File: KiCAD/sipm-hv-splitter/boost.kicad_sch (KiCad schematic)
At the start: 52 parts, among them Q3 BSS138, Q4 BSS138, Q5 BSS138, U2 LT3014xS5, U3 INA201, U4 AD5270

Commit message: working on SiPM power supply schem
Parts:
- C1: renamed from C6; value 0.1uF -> 4.7uF; footprint (none) -> Capacitor_SMD:C_0603_1608Metric_Pad1.08x0.95mm_HandSolder
- C10: renamed from C8; value 0.1uF -> 0.1uF 100V; footprint (none) -> Capacitor_SMD:C_0603_1608Metric_Pad1.08x0.95mm_HandSolder
- C2: value 0.1uF -> 1.0uF; footprint (none) -> Capacitor_SMD:C_0603_1608Metric_Pad1.08x0.95mm_HandSolder
- C3: renamed from C1; value 0.1uF -> 1.0uF; footprint (none) -> Capacitor_SMD:C_0603_1608Metric_Pad1.08x0.95mm_HandSolder
- C4: renamed from C3; value C -> 12nF; footprint (none) -> Capacitor_SMD:C_0603_1608Metric_Pad1.08x0.95mm_HandSolder
- C6: renamed from C10; value C -> 1.0uF
- C7: renamed from C4; value C -> 22nF; footprint (none) -> Capacitor_SMD:C_0603_1608Metric_Pad1.08x0.95mm_HandSolder
- C8: renamed from C5; value C -> 56pF; footprint (none) -> Capacitor_SMD:C_0603_1608Metric_Pad1.08x0.95mm_HandSolder
- C9: renamed from C7; value 3.3uF -> 4.7uF 100V; footprint (none) -> Capacitor_SMD:C_0603_1608Metric_Pad1.08x0.95mm_HandSolder
- D1: value D_Schottky -> MBR1H100SFT3G; footprint (none) -> Diode_SMD:Nexperia_CFP3_SOD-123W; CatNo (none) -> MBR1H100SFT3GOSCT-ND; MfgNo (none) -> MBR1H100SFT3G
- L1: footprint (none) -> my_SMT_Ind:WE-TPC-ind; CatNo (none) -> 732-2617-1-ND; MfgNo (none) -> 744025100
- R10: renamed from R14; value R -> 100; CatNo 311-0.0GRCT-ND -> (none); MfgNo RC0603JR-070RL -> (none)
- R12: renamed from R3; value R_US -> 3.16k; footprint (none) -> Resistor_SMD:R_0603_1608Metric_Pad0.98x0.95mm_HandSolder
- R13: renamed from R4; value R_US -> 150k; footprint (none) -> Resistor_SMD:R_0603_1608Metric_Pad0.98x0.95mm_HandSolder
- R14: renamed from R5; value R_US -> 2.49k; footprint (none) -> Resistor_SMD:R_0603_1608Metric_Pad0.98x0.95mm_HandSolder
- R18: renamed from R9; value 200k 1% -> 510k 1%; CatNo 311-100KHRCT-ND -> (none); MfgNo RC0603FR-07100KL -> (none)
- R19: renamed from R10; value 10.0k 1% -> 24.0k 1%; CatNo 311-10.0KHRCT-ND -> (none); MfgNo RC0603FR-0710KL -> (none)
- R6: renamed from R2; value R_US -> 9.76k; footprint (none) -> Resistor_SMD:R_0603_1608Metric_Pad0.98x0.95mm_HandSolder
- R7: renamed from R18; footprint (none) -> Resistor_SMD:R_0603_1608Metric_Pad0.98x0.95mm_HandSolder
- R8: renamed from R13; value R -> 100; CatNo 311-0.0GRCT-ND -> (none); MfgNo RC0603JR-070RL -> (none)
- U3: renamed from U1; value ~ -> LM51581; footprint (none) -> my_Boost_QFN:QFN-16_EP_3x3_Pitch0.5mm
- renumbered C9 to C11, C11 to C12, C12 to C13, C13 to C14, C14 to C15, C9 to C5, Q5 to Q1, Q3 to Q2, Q4 to Q3, R7 to R11, R6 to R15, R8 to R16, R9 to R17, R11 to R2, R17 to R20, R12 to R3, R16 to R4, R15 to R5, R6 to R9, TP7 to TP1, TP5 to TP2, TP8 to TP3, TP3 to TP4, TP2 to TP5, TP1 to TP6, TP6 to TP7, TP4 to TP8, U3 to U2, U2 to U4, U4 to U5

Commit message: starting placement
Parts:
- C4: value 12nF -> 0.1uF
- R6: value 9.76k -> 10k
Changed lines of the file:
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@@
 			)
 		)
-		(property "Value" "9.76k"
+		(property "Value" "10k"
 			(at 55.88 172.7199 0)
 			(effects
@@
 			)
 		)
-		(property "Value" "12nF"
+		(property "Value" "0.1uF"
 			(at 64.77 172.7262 0)
 			(effects

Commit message: add ISP
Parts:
- C10: footprint Capacitor_SMD:C_0603_1608Metric_Pad1.08x0.95mm_HandSolder -> Capacitor_SMD:C_1206_3216Metric_Pad1.33x1.80mm_HandSolder
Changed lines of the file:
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@@
 			)
 		)
-		(property "Footprint" "Capacitor_SMD:C_0603_1608Metric_Pad1.08x0.95mm_HandSolder"
+		(property "Footprint" "Capacitor_SMD:C_1206_3216Metric_Pad1.33x1.80mm_HandSolder"
 			(at 133.35 146.05 0)
 			(effects

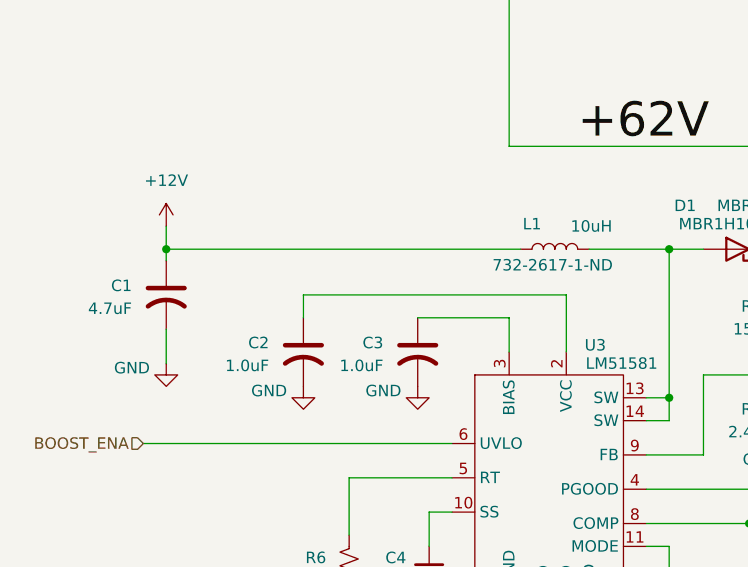
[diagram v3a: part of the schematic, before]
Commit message: working on 2.5 in placement
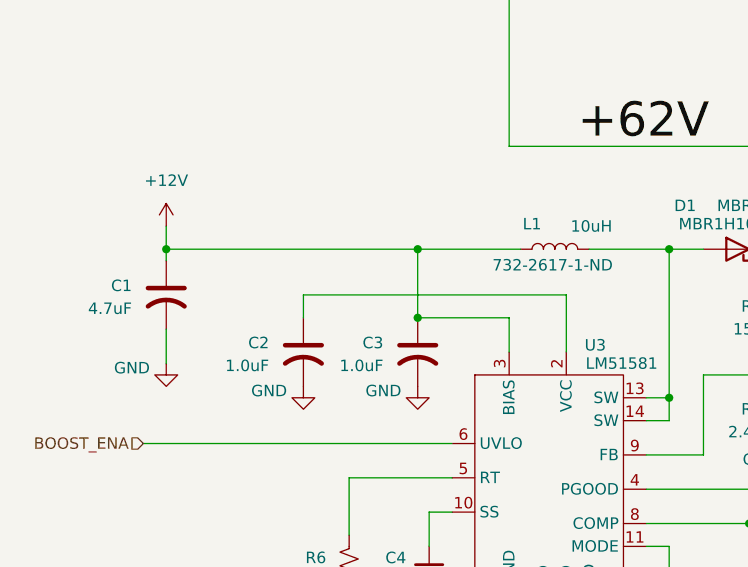
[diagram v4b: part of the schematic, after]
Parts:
- C10: footprint Capacitor_SMD:C_1206_3216Metric_Pad1.33x1.80mm_HandSolder -> Capacitor_SMD:C_0603_1608Metric_Pad1.08x0.95mm_HandSolder
- C9: footprint Capacitor_SMD:C_0603_1608Metric_Pad1.08x0.95mm_HandSolder -> Capacitor_SMD:C_1206_3216Metric_Pad1.33x1.80mm_HandSolder
- R9: footprint Resistor_SMD:R_0603_1608Metric_Pad0.98x0.95mm_HandSolder -> Resistor_SMD:R_1206_3216Metric_Pad1.30x1.75mm_HandSolder
- TP1, TP2, TP3, TP4, TP5, TP6, TP7, TP8: footprint my_tp:tp_SMT_label2 -> TestPoint:TestPoint_Pad_D2.0mm
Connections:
- net +12V: now also C3.1, U3.3 (BIAS)
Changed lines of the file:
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@@
 	)
 	(junction
+		(at 66.04 143.51)
+		(diameter 0)
+		(color 0 0 0 0)
+	)
+	(junction
 		(at 233.68 49.53)
 		(diameter 0)
@@
 	)
 	(junction
+		(at 66.04 135.89)
+		(diameter 0)
+		(color 0 0 0 0)
+	)
+	(junction
 		(at 243.84 41.91)
 		(diameter 0)
@@
 	(wire
 		(pts
+			(xy 66.04 135.89) (xy 77.47 135.89)
+		)
+		(stroke
+			(width 0)
+			(type default)
+		)
+	)
+	(wire
+		(pts
 			(xy 53.34 140.97) (xy 82.55 140.97)
 		)
@@
 	(wire
 		(pts
-			(xy 38.1 135.89) (xy 77.47 135.89)
+			(xy 38.1 135.89) (xy 66.04 135.89)
 		)
 		(stroke
@@
 	(wire
 		(pts
+			(xy 66.04 135.89) (xy 66.04 143.51)
+		)
+		(stroke
+			(width 0)
+			(type default)
+		)
+	)
+	(wire
+		(pts
 			(xy 53.34 44.45) (xy 53.34 66.04)
 		)
@@
 			)
 		)
-		(property "Footprint" "my_tp:tp_SMT_label2"
+		(property "Footprint" "TestPoint:TestPoint_Pad_D2.0mm"
 			(at 248.92 38.1 0)
 			(effects
@@
 			)
 		)
-		(property "Footprint" "Capacitor_SMD:C_1206_3216Metric_Pad1.33x1.80mm_HandSolder"
+		(property "Footprint" "Capacitor_SMD:C_0603_1608Metric_Pad1.08x0.95mm_HandSolder"
 			(at 133.35 146.05 0)
 			(effects
@@
 			)
 		)
-		(property "Footprint" "my_tp:tp_SMT_label2"
+		(property "Footprint" "TestPoint:TestPoint_Pad_D2.0mm"
 			(at 104.14 58.42 0)
 			(effects
@@
 			)
 		)
-		(property "Footprint" "my_tp:tp_SMT_label2"
+		(property "Footprint" "TestPoint:TestPoint_Pad_D2.0mm"
 			(at 81.28 88.9 0)
 			(effects
@@
 			)
 		)
-		(property "Footprint" "my_tp:tp_SMT_label2"
+		(property "Footprint" "TestPoint:TestPoint_Pad_D2.0mm"
 			(at 236.22 113.03 0)
 			(effects
@@
 			)
 		)
-		(property "Footprint" "my_tp:tp_SMT_label2"
+		(property "Footprint" "TestPoint:TestPoint_Pad_D2.0mm"
 			(at 228.6 52.07 0)
 			(effects
@@
 			)
 		)
-		(property "Footprint" "Resistor_SMD:R_0603_1608Metric_Pad0.98x0.95mm_HandSolder"
+		(property "Footprint" "Resistor_SMD:R_1206_3216Metric_Pad1.30x1.75mm_HandSolder"
 			(at 91.694 97.536 90)
 			(effects
@@
 			)
 		)
-		(property "Footprint" "Capacitor_SMD:C_0603_1608Metric_Pad1.08x0.95mm_HandSolder"
+		(property "Footprint" "Capacitor_SMD:C_1206_3216Metric_Pad1.33x1.80mm_HandSolder"
 			(at 120.65 146.05 0)
 			(effects
@@
 			)
 		)
-		(property "Footprint" "my_tp:tp_SMT_label2"
+		(property "Footprint" "TestPoint:TestPoint_Pad_D2.0mm"
 			(at 185.42 59.69 0)
 			(effects
@@
 			)
 		)
-		(property "Footprint" "my_tp:tp_SMT_label2"
+		(property "Footprint" "TestPoint:TestPoint_Pad_D2.0mm"
 			(at 33.02 41.91 0)
 			(effects
@@
 			)
 		)
-		(property "Footprint" "my_tp:tp_SMT_label2"
+		(property "Footprint" "TestPoint:TestPoint_Pad_D2.0mm"
 			(at 109.22 88.9 0)
 			(effects

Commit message: routing madness
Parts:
- C15: now fitted
- TP1, TP2, TP3, TP4, TP5, TP6, TP7, TP8: footprint TestPoint:TestPoint_Pad_D2.0mm -> TestPoint:TestPoint_Pad_D1.0mm; now fitted; now left out of the parts list
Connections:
- net V62_IN: now reaches C11.1, R10.2, R9.2, TP4.1, U4.1 (VIN)
- net +62V renamed 62V
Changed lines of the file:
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@@
 		)
 	)
+	(label "V62_IN"
+		(at 114.3 92.71 0)
+		(effects
+			(font
+				(size 1.27 1.27)
+			)
+			(justify left bottom)
+		)
+	)
 	(label "IMON"
 		(at 46.99 48.26 0)
@@
 		)
 	)
-	(label "+62V"
+	(label "62V"
 		(at 83.82 124.46 0)
 		(effects
@@
 		(unit 1)
 		(exclude_from_sim no)
-		(in_bom yes)
+		(in_bom no)
 		(on_board yes)
-		(dnp yes)
+		(dnp no)
 		(property "Reference" "TP8"
 			(at 238.506 32.258 0)
@@
 			)
 		)
-		(property "Footprint" "TestPoint:TestPoint_Pad_D2.0mm"
+		(property "Footprint" "TestPoint:TestPoint_Pad_D1.0mm"
 			(at 248.92 38.1 0)
 			(effects
@@
 		(in_bom no)
 		(on_board yes)
-		(dnp yes)
+		(dnp no)
 		(property "Reference" "C15"
 			(at 236.22 93.9799 0)
@@
 		(unit 1)
 		(exclude_from_sim no)
-		(in_bom yes)
+		(in_bom no)
 		(on_board yes)
-		(dnp yes)
+		(dnp no)
 		(property "Reference" "TP3"
 			(at 101.6 62.9921 0)
@@
 			)
 		)
-		(property "Footprint" "TestPoint:TestPoint_Pad_D2.0mm"
+		(property "Footprint" "TestPoint:TestPoint_Pad_D1.0mm"
 			(at 104.14 58.42 0)
 			(effects
@@
 		(unit 1)
 		(exclude_from_sim no)
-		(in_bom yes)
+		(in_bom no)
 		(on_board yes)
-		(dnp yes)
+		(dnp no)
 		(property "Reference" "TP2"
 			(at 71.628 88.392 0)
@@
 			)
 		)
-		(property "Footprint" "TestPoint:TestPoint_Pad_D2.0mm"
+		(property "Footprint" "TestPoint:TestPoint_Pad_D1.0mm"
 			(at 81.28 88.9 0)
 			(effects
@@
 		(unit 1)
 		(exclude_from_sim no)
-		(in_bom yes)
+		(in_bom no)
 		(on_board yes)
-		(dnp yes)
+		(dnp no)
 		(fields_autoplaced yes)
 		(property "Reference" "TP6"
@@
 			)
 		)
-		(property "Footprint" "TestPoint:TestPoint_Pad_D2.0mm"
+		(property "Footprint" "TestPoint:TestPoint_Pad_D1.0mm"
 			(at 236.22 113.03 0)
 			(effects
@@
 		(unit 1)
 		(exclude_from_sim no)
-		(in_bom yes)
+		(in_bom no)
 		(on_board yes)
-		(dnp yes)
+		(dnp no)
 		(property "Reference" "TP7"
 			(at 239.776 54.356 0)
@@
 			)
 		)
-		(property "Footprint" "TestPoint:TestPoint_Pad_D2.0mm"
+		(property "Footprint" "TestPoint:TestPoint_Pad_D1.0mm"
 			(at 228.6 52.07 0)
 			(effects
@@
 		(unit 1)
 		(exclude_from_sim no)
-		(in_bom yes)
+		(in_bom no)
 		(on_board yes)
-		(dnp yes)
+		(dnp no)
 		(fields_autoplaced yes)
 		(property "Reference" "TP5"
@@
 			)
 		)
-		(property "Footprint" "TestPoint:TestPoint_Pad_D2.0mm"
+		(property "Footprint" "TestPoint:TestPoint_Pad_D1.0mm"
 			(at 185.42 59.69 0)
 			(effects
@@
 		(unit 1)
 		(exclude_from_sim no)
-		(in_bom yes)
+		(in_bom no)
 		(on_board yes)
-		(dnp yes)
+		(dnp no)
 		(property "Reference" "TP1"
 			(at 35.56 37.3379 0)
@@
 			)
 		)
-		(property "Footprint" "TestPoint:TestPoint_Pad_D2.0mm"
+		(property "Footprint" "TestPoint:TestPoint_Pad_D1.0mm"
 			(at 33.02 41.91 0)
 			(effects
@@
 		(unit 1)
 		(exclude_from_sim no)
-		(in_bom yes)
+		(in_bom no)
 		(on_board yes)
-		(dnp yes)
+		(dnp no)
 		(property "Reference" "TP4"
 			(at 99.568 87.63 0)
@@
 			)
 		)
-		(property "Footprint" "TestPoint:TestPoint_Pad_D2.0mm"
+		(property "Footprint" "TestPoint:TestPoint_Pad_D1.0mm"
 			(at 109.22 88.9 0)
 			(effects

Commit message: working on bias filter changes
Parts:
- C1, C10, C2, C3, C9: symbol Device:C_US -> Device:C
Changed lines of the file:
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@@
 	)
 	(symbol
-		(lib_id "Device:C_US")
+		(lib_id "Device:C")
 		(at 133.35 146.05 0)
 		(unit 1)
@@
 		)
 		(property "Footprint" "Capacitor_SMD:C_0603_1608Metric_Pad1.08x0.95mm_HandSolder"
-			(at 133.35 146.05 0)
+			(at 134.3152 149.86 0)
 			(effects
 				(font
@@
 			)
 		)
-		(property "Datasheet" ""
+		(property "Datasheet" "~"
 			(at 133.35 146.05 0)
 			(effects
@@
 			)
 		)
-		(property "Description" "capacitor, US symbol"
+		(property "Description" "Unpolarized capacitor"
 			(at 133.35 146.05 0)
 			(effects
@@
 	)
 	(symbol
-		(lib_id "Device:C_US")
+		(lib_id "Device:C")
 		(at 38.1 140.97 0)
 		(unit 1)
@@
 		)
 		(property "Footprint" "Capacitor_SMD:C_0603_1608Metric_Pad1.08x0.95mm_HandSolder"
-			(at 38.1 140.97 0)
+			(at 39.0652 144.78 0)
 			(effects
 				(font
@@
 			)
 		)
-		(property "Datasheet" ""
+		(property "Datasheet" "~"
 			(at 38.1 140.97 0)
 			(effects
@@
 			)
 		)
-		(property "Description" "capacitor, US symbol"
+		(property "Description" "Unpolarized capacitor"
 			(at 38.1 140.97 0)
 			(effects
@@
 	)
 	(symbol
-		(lib_id "Device:C_US")
+		(lib_id "Device:C")
 		(at 120.65 146.05 0)
 		(unit 1)
@@
 		)
 		(property "Footprint" "Capacitor_SMD:C_1206_3216Metric_Pad1.33x1.80mm_HandSolder"
-			(at 120.65 146.05 0)
+			(at 121.6152 149.86 0)
 			(effects
 				(font
@@
 			)
 		)
-		(property "Datasheet" ""
+		(property "Datasheet" "~"
 			(at 120.65 146.05 0)
 			(effects
@@
 			)
 		)
-		(property "Description" "capacitor, US symbol"
+		(property "Description" "Unpolarized capacitor"
 			(at 120.65 146.05 0)
 			(effects
@@
 	)
 	(symbol
-		(lib_id "Device:C_US")
+		(lib_id "Device:C")
 		(at 53.34 147.32 0)
 		(unit 1)
@@
 		)
 		(property "Footprint" "Capacitor_SMD:C_0603_1608Metric_Pad1.08x0.95mm_HandSolder"
-			(at 53.34 147.32 0)
+			(at 54.3052 151.13 0)
 			(effects
 				(font
@@
 			)
 		)
-		(property "Datasheet" ""
+		(property "Datasheet" "~"
 			(at 53.34 147.32 0)
 			(effects
@@
 			)
 		)
-		(property "Description" "capacitor, US symbol"
+		(property "Description" "Unpolarized capacitor"
 			(at 53.34 147.32 0)
 			(effects
@@
 	)
 	(symbol
-		(lib_id "Device:C_US")
+		(lib_id "Device:C")
 		(at 66.04 147.32 0)
 		(unit 1)
@@
 		)
 		(property "Footprint" "Capacitor_SMD:C_0603_1608Metric_Pad1.08x0.95mm_HandSolder"
-			(at 66.04 147.32 0)
+			(at 67.0052 151.13 0)
 			(effects
 				(font
@@
 			)
 		)
-		(property "Datasheet" ""
+		(property "Datasheet" "~"
 			(at 66.04 147.32 0)
 			(effects
@@
 			)
 		)
-		(property "Description" "capacitor, US symbol"
+		(property "Description" "Unpolarized capacitor"
 			(at 66.04 147.32 0)
 			(effects

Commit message: working on BOM
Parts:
- C1: CatNo (none) -> 1276-1784-1-ND; MfgNo (none) -> CL10A475KO8NNNC
- C10: CatNo (none) -> 1276-6807-1-ND; MfgNo (none) -> CL10B104KC8NNNC
- C13, C5: CatNo 399-C0603C103M4REC7411CT-ND -> 478-KGF15AR71H103MTCT-ND; MfgNo C0603C103M4REC7411 -> 06035C103MAZ2A
- C2, C3, C6: CatNo (none) -> 1276-1019-1-ND; MfgNo (none) -> CL10B105KO8NNNC
- C4: CatNo (none) -> 311-1088-1-ND; MfgNo (none) -> CC0603KRX7R7BB104
- C7: CatNo (none) -> 1292-1415-1-ND; MfgNo (none) -> 0603B223K160CT
- C8: CatNo (none) -> 478-600S560JT250XT4KCT-ND; MfgNo (none) -> 600S560JT250XT4K
- C9: CatNo (none) -> 490-18620-1-ND; MfgNo (none) -> GRM31CC72A475KE11L
- R10, R8: CatNo (none) -> P100HCT-ND; MfgNo (none) -> ERJ-3EKF1000V
- R16, R5: value 10.0k 1% -> 10k
- R6: CatNo (none) -> 311-10.0KHRCT-ND; MfgNo (none) -> RC0603FR-0710KL
- R7: CatNo (none) -> 541-100KHCT-ND; MfgNo (none) -> CRCW0603100KFKEA
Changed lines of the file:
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@@
 			)
 		)
-		(property "MfgNo" "C0603C103M4REC7411"
+		(property "MfgNo" "06035C103MAZ2A"
 			(at 199.39 97.79 0)
 			(effects
@@
 			)
 		)
-		(property "CatNo" "399-C0603C103M4REC7411CT-ND"
+		(property "CatNo" "478-KGF15AR71H103MTCT-ND"
 			(at 199.39 97.79 0)
 			(effects
@@
 			)
 		)
+		(property "CatNo" "478-600S560JT250XT4KCT-ND"
+			(at 107.95 177.8 0)
+			(effects
+				(font
+					(size 1.27 1.27)
+				)
+				(hide yes)
+			)
+		)
+		(property "MfgNo" "600S560JT250XT4K"
+			(at 107.95 177.8 0)
+			(effects
+				(font
+					(size 1.27 1.27)
+				)
+				(hide yes)
+			)
+		)
 		(pin "1"
 		)
@@
 			)
 		)
+		(property "CatNo" "311-10.0KHRCT-ND"
+			(at 58.42 171.45 0)
+			(effects
+				(font
+					(size 1.27 1.27)
+				)
+				(hide yes)
+			)
+		)
+		(property "MfgNo" "RC0603FR-0710KL"
+			(at 58.42 171.45 0)
+			(effects
+				(font
+					(size 1.27 1.27)
+				)
+				(hide yes)
+			)
+		)
 		(pin "1"
 		)
@@
 			)
 		)
+		(property "CatNo" "1292-1415-1-ND"
+			(at 102.87 182.88 0)
+			(effects
+				(font
+					(size 1.27 1.27)
+				)
+				(hide yes)
+			)
+		)
+		(property "MfgNo" "0603B223K160CT"
+			(at 102.87 182.88 0)
+			(effects
+				(font
+					(size 1.27 1.27)
+				)
+				(hide yes)
+			)
+		)
 		(pin "1"
 		)
@@
 			)
 		)
+		(property "CatNo" "1276-6807-1-ND"
+			(at 133.35 146.05 0)
+			(effects
+				(font
+					(size 1.27 1.27)
+				)
+				(hide yes)
+			)
+		)
+		(property "MfgNo" "CL10B104KC8NNNC"
+			(at 133.35 146.05 0)
+			(effects
+				(font
+					(size 1.27 1.27)
+				)
+				(hide yes)
+			)
+		)
 		(pin "1"
 		)
@@
 			)
 		)
-		(property "MfgNo" ""
+		(property "MfgNo" "ERJ-3EKF1000V"
 			(at 95.25 77.47 0)
 			(effects
@@
 			)
 		)
-		(property "CatNo" ""
+		(property "CatNo" "P100HCT-ND"
 			(at 95.25 77.47 0)
 			(effects
@@
 			)
 		)
+		(property "CatNo" "1276-1784-1-ND"
+			(at 38.1 140.97 0)
+			(effects
+				(font
+					(size 1.27 1.27)
+				)
+				(hide yes)
+			)
+		)
+		(property "MfgNo" "CL10A475KO8NNNC"
+			(at 38.1 140.97 0)
+			(effects
+				(font
+					(size 1.27 1.27)
+				)
+				(hide yes)
+			)
+		)
 		(pin "1"
 		)
@@
 			)
 		)
-		(property "MfgNo" ""
+		(property "MfgNo" "ERJ-3EKF1000V"
 			(at 87.63 77.47 0)
 			(effects
@@
 			)
 		)
-		(property "CatNo" ""
+		(property "CatNo" "P100HCT-ND"
 			(at 87.63 77.47 0)
 			(effects
@@
 			)
 		)
-		(property "MfgNo" "C0603C103M4REC7411"
+		(property "MfgNo" "06035C103MAZ2A"
 			(at 76.2 31.75 0)
 			(effects
@@
 			)
 		)
-		(property "CatNo" "399-C0603C103M4REC7411CT-ND"
+		(property "CatNo" "478-KGF15AR71H103MTCT-ND"
 			(at 76.2 31.75 0)
 			(effects
@@
 			)
 		)
+		(property "CatNo" "490-18620-1-ND"
+			(at 120.65 146.05 0)
+			(effects
+				(font
+					(size 1.27 1.27)
+				)
+				(hide yes)
+			)
+		)
+		(property "MfgNo" "GRM31CC72A475KE11L"
+			(at 120.65 146.05 0)
+			(effects
+				(font
+					(size 1.27 1.27)
+				)
+				(hide yes)
+			)
+		)
 		(pin "1"
 		)
@@
 		(fields_autoplaced yes)
 		(property "Reference" "R16"
-			(at 119.38 43.1799 0)
+			(at 124.46 43.1799 0)
 			(effects
 				(font
 					(size 1.27 1.27)
 				)
-				(justify left)
+				(justify right)
 			)
 		)
-		(property "Value" "10.0k 1%"
-			(at 119.38 45.7199 0)
+		(property "Value" "10k"
+			(at 124.46 45.7199 0)
 			(effects
 				(font
 					(size 1.27 1.27)
 				)
-				(justify left)
+				(justify right)
 			)
 		)
@@
 			)
 		)
+		(property "CatNo" "311-1088-1-ND"
+			(at 67.31 171.45 0)
+			(effects
+				(font
+					(size 1.27 1.27)
+				)
+				(hide yes)
+			)
+		)
+		(property "MfgNo" "CC0603KRX7R7BB104"
+			(at 67.31 171.45 0)
+			(effects
+				(font
+					(size 1.27 1.27)
+				)
+				(hide yes)
+			)
+		)
 		(pin "1"
 		)
@@
 			)
 		)
+		(property "CatNo" "1276-1019-1-ND"
+			(at 53.34 147.32 0)
+			(effects
+				(font
+					(size 1.27 1.27)
+				)
+				(hide yes)
+			)
+		)
+		(property "MfgNo" "CL10B105KO8NNNC"
+			(at 53.34 147.32 0)
+			(effects
+				(font
+					(size 1.27 1.27)
+				)
+				(hide yes)
+			)
+		)
 		(pin "1"
 		)
@@
 			)
 		)
+		(property "CatNo" "541-100KHCT-ND"
+			(at 60.96 101.6 0)
+			(effects
+				(font
+					(size 1.27 1.27)
+				)
+				(hide yes)
+			)
+		)
+		(property "MfgNo" "CRCW0603100KFKEA"
+			(at 60.96 101.6 0)
+			(effects
+				(font
+					(size 1.27 1.27)
+				)
+				(hide yes)
+			)
+		)
 		(pin "1"
 		)
@@
 			)
 		)
+		(property "CatNo" "1276-1019-1-ND"
+			(at 66.04 147.32 0)
+			(effects
+				(font
+					(size 1.27 1.27)
+				)
+				(hide yes)
+			)
+		)
+		(property "MfgNo" "CL10B105KO8NNNC"
+			(at 66.04 147.32 0)
+			(effects
+				(font
+					(size 1.27 1.27)
+				)
+				(hide yes)
+			)
+		)
 		(pin "1"
 		)
@@
 			)
 		)
-		(property "Value" "10.0k 1%"
+		(property "Value" "10k"
 			(at 52.832 43.434 0)
 			(effects
@@
 			)
 		)
-		(property "MfgNo" ""
+		(property "MfgNo" "CL10B105KO8NNNC"
+			(at 91.44 71.12 90)
+			(effects
+				(font
+					(size 1.27 1.27)
+				)
+				(hide yes)
+			)
+		)
+		(property "CatNo" "1276-1019-1-ND"
 			(at 91.44 71.12 90)
 			(effects
